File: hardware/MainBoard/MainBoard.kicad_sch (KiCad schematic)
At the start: 8 parts, among them J1 MPU9250, J2 Micro_SD_Card, J3 Servo, J4 Relay, J5 MotorDriver, J6 PicoBATT+, J7 Tachometer

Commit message: 色々つけて、フットプリント割り当てた。
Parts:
- removed J2: Micro_SD_Card, symbol Connector:Micro_SD_Card
- added D101: Relay, LED_THT:LED_D3.0mm, symbol Device:LED
- added D102: STAT, LED_THT:LED_D3.0mm, symbol Device:LED
- added D103: ERROR, LED_THT:LED_D3.0mm, symbol Device:LED
- added D104: VPP, LED_THT:LED_D3.0mm, symbol Device:LED
- added D105: VDD, LED_THT:LED_D3.0mm, symbol Device:LED
- added R101, R102, R103, R104, R105: 1k, Resistor_THT:R_Axial_DIN0204_L3.6mm_D1.6mm_P5.08mm_Horizontal, symbol Device:R
- added SW101: Reset, Button_Switch_THT:SW_PUSH_6mm, symbol Switch:SW_Push
- added SW102: SW_Pico, Button_Switch_THT:SW_Slide_SPDT_Angled_CK_OS102011MA1Q, symbol Switch:SW_SPDT
- added SW103: SW_BATT, Button_Switch_THT:SW_Slide_SPDT_Angled_CK_OS102011MA1Q, symbol Switch:SW_SPDT
- J101: renamed from J3; footprint (none) -> Connector_JST:JST_XH_B3B-XH-A_1x03_P2.50mm_Vertical
- J102: renamed from J4; footprint (none) -> Connector_JST:JST_XH_B3B-XH-A_1x03_P2.50mm_Vertical
- J103: renamed from J5; footprint (none) -> Connector_JST:JST_XH_B5B-XH-A_1x05_P2.50mm_Vertical
- J104: renamed from J1; footprint (none) -> Connector_JST:JST_XH_B10B-XH-A_1x10_P2.50mm_Vertical
- J105: renamed from J6; footprint (none) -> Connector_JST:JST_PH_B2B-PH-K_1x02_P2.00mm_Vertical
- J106: renamed from J7; footprint (none) -> Connector_JST:JST_XH_B4B-XH-A_1x04_P2.50mm_Vertical
- renumbered A1 to A101
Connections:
- net GND: now also R101.1, R102.1, R103.2, R104.2, R105.2, SW101.1, SW102.2 (B)
- net OUT1: now also A101.26 (GPIO20); no longer A101.29 (GPIO22)
- net OUT2: now also A101.27 (GPIO21); no longer A101.31 (GPIO26_ADC0)
- net Relay_S: now also D101.2 (A)
- net VDD: now also D105.2 (A)
- net at J105.1 (Pin_1): now also D104.2 (A), SW103.1 (A); no longer A101.39 (VSYS)
- net ERROR: now reaches A101.10 (GPIO7)
- net ERROR: now also D103.2 (A)
- net at A101.30 (RUN): now also SW101.2
- net at A101.37 (3V3_EN): now also SW102.1 (A)
- net STAT: now reaches A101.9 (GPIO6)
- net STAT: now also D102.2 (A)
- new net: D105.1 (K), R105.1
- new net: D103.1 (K), R103.1
- new net: D102.1 (K), R102.2
- new net: D101.1 (K), R101.2
- new net: D104.1 (K), R104.1
- new net: A101.39 (VSYS), SW103.2 (B)
- no-connect marks 21 -> 16
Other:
- added sheet microSD (untitled.kicad_sch)
- moved on the sheet: A101, J101, J102, J103, J104, J105, J106

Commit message: PCB途中
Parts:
- added B101: ~, WOBCLibrary:Board_1U_60x60, symbol WOBCLibrary:Board
- J104: footprint Connector_JST:JST_XH_B10B-XH-A_1x10_P2.50mm_Vertical -> Connector_PinSocket_2.54mm:PinSocket_1x10_P2.54mm_Vertical
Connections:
- net GND: now also B101.GND
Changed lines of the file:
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@@
 	(wire
 		(pts
+			(xy 45.72 33.02) (xy 59.69 33.02)
+		)
+		(stroke
+			(width 0)
+			(type default)
+		)
+	)
+	(wire
+		(pts
 			(xy 201.93 113.03) (xy 201.93 123.19)
 		)
@@
 	(wire
 		(pts
+			(xy 59.69 33.02) (xy 59.69 40.64)
+		)
+		(stroke
+			(width 0)
+			(type default)
+		)
+	)
+	(wire
+		(pts
 			(xy 93.98 110.49) (xy 121.92 110.49)
 		)
@@
 	(wire
 		(pts
+			(xy 45.72 40.64) (xy 45.72 33.02)
+		)
+		(stroke
+			(width 0)
+			(type default)
+		)
+	)
+	(wire
+		(pts
 			(xy 167.64 90.17) (xy 179.07 90.17)
 		)
@@
 	)
 	(symbol
+		(lib_id "WOBCLibrary:Board")
+		(at 45.72 40.64 0)
+		(unit 1)
+		(exclude_from_sim no)
+		(in_bom yes)
+		(on_board yes)
+		(dnp no)
+		(fields_autoplaced yes)
+		(property "Reference" "B101"
+			(at 48.26 40.4367 0)
+			(effects
+				(font
+					(size 1.27 1.27)
+				)
+				(justify left)
+			)
+		)
+		(property "Value" "~"
+			(at 48.26 42.9767 0)
+			(effects
+				(font
+					(size 1.27 1.27)
+				)
+				(justify left)
+			)
+		)
+		(property "Footprint" "WOBCLibrary:Board_1U_60x60"
+			(at 45.72 40.64 0)
+			(effects
+				(font
+					(size 1.27 1.27)
+				)
+				(hide yes)
+			)
+		)
+		(property "Datasheet" ""
+			(at 45.72 40.64 0)
+			(effects
+				(font
+					(size 1.27 1.27)
+				)
+				(hide yes)
+			)
+		)
+		(property "Description" ""
+			(at 45.72 40.64 0)
+			(effects
+				(font
+					(size 1.27 1.27)
+				)
+				(hide yes)
+			)
+		)
+		(pin "GND"
+		)
+		(instances
+			(project ""
+				(path "/11ae0773-063e-421c-b359-668d7833fea8"
+					(reference "B101")
+					(unit 1)
+				)
+			)
+		)
+	)
+	(symbol
 		(lib_id "power:GND")
 		(at 191.77 111.76 0)
@@
 	)
 	(symbol
+		(lib_id "power:GND")
+		(at 59.69 40.64 0)
+		(unit 1)
+		(exclude_from_sim no)
+		(in_bom yes)
+		(on_board yes)
+		(dnp no)
+		(fields_autoplaced yes)
+		(property "Reference" "#PWR0206"
+			(at 59.69 46.99 0)
+			(effects
+				(font
+					(size 1.27 1.27)
+				)
+				(hide yes)
+			)
+		)
+		(property "Value" "GND"
+			(at 59.69 45.72 0)
+			(effects
+				(font
+					(size 1.27 1.27)
+				)
+			)
+		)
+		(property "Footprint" ""
+			(at 59.69 40.64 0)
+			(effects
+				(font
+					(size 1.27 1.27)
+				)
+				(hide yes)
+			)
+		)
+		(property "Datasheet" ""
+			(at 59.69 40.64 0)
+			(effects
+				(font
+					(size 1.27 1.27)
+				)
+				(hide yes)
+			)
+		)
+		(property "Description" "Power symbol creates a global label with name \"GND\" , ground"
+			(at 59.69 40.64 0)
+			(effects
+				(font
+					(size 1.27 1.27)
+				)
+				(hide yes)
+			)
+		)
+		(pin "1"
+		)
+		(instances
+			(project ""
+				(path "/11ae0773-063e-421c-b359-668d7833fea8"
+					(reference "#PWR0206")
+					(unit 1)
+				)
+			)
+		)
+	)
+	(symbol
 		(lib_id "Connector_Generic:Conn_01x10")
 		(at 124.46 147.32 0)
@@
 			)
 		)
-		(property "Footprint" "Connector_JST:JST_XH_B10B-XH-A_1x10_P2.50mm_Vertical"
+		(property "Footprint" "Connector_PinSocket_2.54mm:PinSocket_1x10_P2.54mm_Vertical"
 			(at 124.46 147.32 0)
 			(effects

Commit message: コネクタ類をまとめた
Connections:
- net CLK: now also A101.22 (GPIO17); no longer A101.24 (GPIO18)
- net CS: now also A101.25 (GPIO19); no longer A101.22 (GPIO17)
- net MOSI: now also A101.24 (GPIO18); no longer A101.25 (GPIO19)
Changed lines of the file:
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@@
-		)
-	)
-	(label "MOSI"
-		(at 196.85 87.63 180)
-		(effects
-			(font
-				(size 1.27 1.27)
-			)
-			(justify right bottom)
 		)
 	)
@@
 		)
 	)
+	(label "CS"
+		(at 196.85 87.63 180)
+		(effects
+			(font
+				(size 1.27 1.27)
+			)
+			(justify right bottom)
+		)
+	)
 	(label "ERROR"
 		(at 59.69 168.91 180)
@@
 		)
 	)
+	(label "MOSI"
+		(at 196.85 85.09 180)
+		(effects
+			(font
+				(size 1.27 1.27)
+			)
+			(justify right bottom)
+		)
+	)
+	(label "IN2"
+		(at 93.98 107.95 0)
+		(effects
+			(font
+				(size 1.27 1.27)
+			)
+			(justify left bottom)
+		)
+	)
+	(label "Servo_S"
+		(at 88.9 127 180)
+		(effects
+			(font
+				(size 1.27 1.27)
+			)
+			(justify right bottom)
+		)
+	)
+	(label "IN1"
+		(at 88.9 93.98 180)
+		(effects
+			(font
+				(size 1.27 1.27)
+			)
+			(justify right bottom)
+		)
+	)
+	(label "Relay_S"
+		(at 59.69 146.05 180)
+		(effects
+			(font
+				(size 1.27 1.27)
+			)
+			(justify right bottom)
+		)
+	)
+	(label "ERROR"
+		(at 114.3 95.25 0)
+		(effects
+			(font
+				(size 1.27 1.27)
+			)
+			(justify left bottom)
+		)
+	)
+	(label "Servo_S"
+		(at 93.98 102.87 0)
+		(effects
+			(font
+				(size 1.27 1.27)
+			)
+			(justify left bottom)
+		)
+	)
+	(label "CS"
+		(at 201.93 73.66 0)
+		(effects
+			(font
+				(size 1.27 1.27)
+			)
+			(justify left bottom)
+		)
+	)
+	(label "STAT"
+		(at 114.3 92.71 0)
+		(effects
+			(font
+				(size 1.27 1.27)
+			)
+			(justify left bottom)
+		)
+	)
+	(label "CLK"
+		(at 196.85 82.55 180)
+		(effects
+			(font
+				(size 1.27 1.27)
+			)
+			(justify right bottom)
+		)
+	)
+	(label "FSYNC"
+		(at 113.03 160.02 0)
+		(effects
+			(font
+				(size 1.27 1.27)
+			)
+			(justify left bottom)
+		)
+	)
 	(label "MISO"
 		(at 196.85 80.01 180)
@@
 		)
 	)
-	(label "IN2"
-		(at 93.98 107.95 0)
-		(effects
-			(font
-				(size 1.27 1.27)
-			)
-			(justify left bottom)
-		)
-	)
-	(label "CS"
-		(at 196.85 82.55 180)
-		(effects
-			(font
-				(size 1.27 1.27)
-			)
-			(justify right bottom)
-		)
-	)
-	(label "Servo_S"
-		(at 88.9 127 180)
-		(effects
-			(font
-				(size 1.27 1.27)
-			)
-			(justify right bottom)
-		)
-	)
-	(label "IN1"
-		(at 88.9 93.98 180)
-		(effects
-			(font
-				(size 1.27 1.27)
-			)
-			(justify right bottom)
-		)
-	)
-	(label "Relay_S"
-		(at 59.69 146.05 180)
-		(effects
-			(font
-				(size 1.27 1.27)
-			)
-			(justify right bottom)
-		)
-	)
-	(label "ERROR"
-		(at 114.3 95.25 0)
-		(effects
-			(font
-				(size 1.27 1.27)
-			)
-			(justify left bottom)
-		)
-	)
-	(label "CLK"
-		(at 196.85 85.09 180)
-		(effects
-			(font
-				(size 1.27 1.27)
-			)
-			(justify right bottom)
-		)
-	)
-	(label "Servo_S"
-		(at 93.98 102.87 0)
-		(effects
-			(font
-				(size 1.27 1.27)
-			)
-			(justify left bottom)
-		)
-	)
-	(label "CS"
-		(at 201.93 73.66 0)
-		(effects
-			(font
-				(size 1.27 1.27)
-			)
-			(justify left bottom)
-		)
-	)
-	(label "STAT"
-		(at 114.3 92.71 0)
-		(effects
-			(font
-				(size 1.27 1.27)
-			)
-			(justify left bottom)
-		)
-	)
-	(label "FSYNC"
-		(at 113.03 160.02 0)
-		(effects
-			(font
-				(size 1.27 1.27)
-			)
-			(justify left bottom)
-		)
-	)

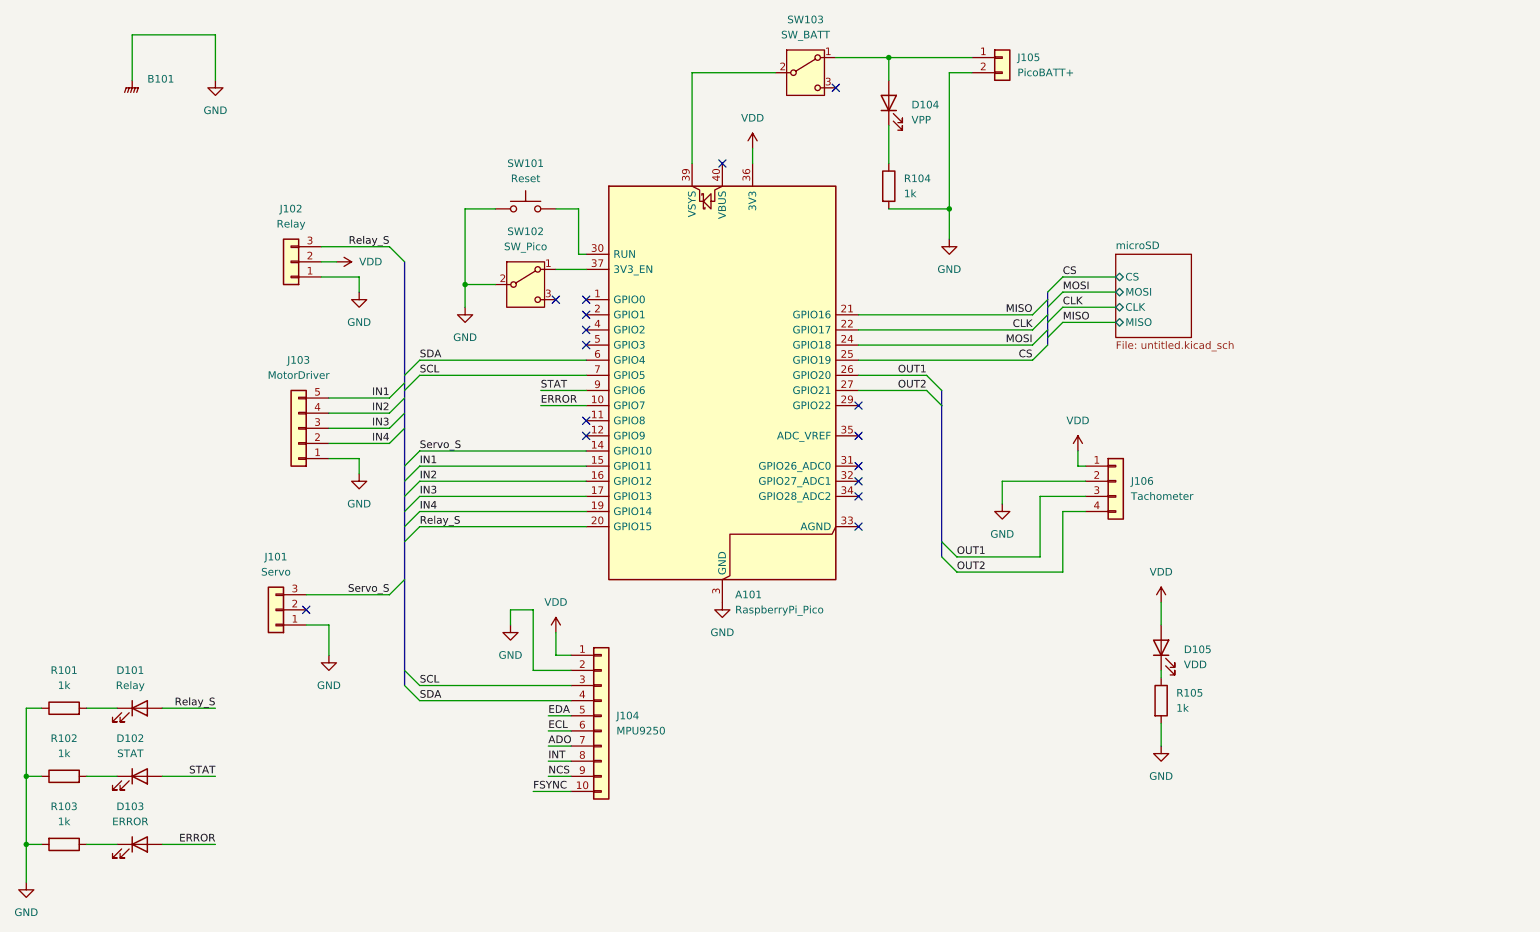
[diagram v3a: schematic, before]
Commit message: PCBで配線少し
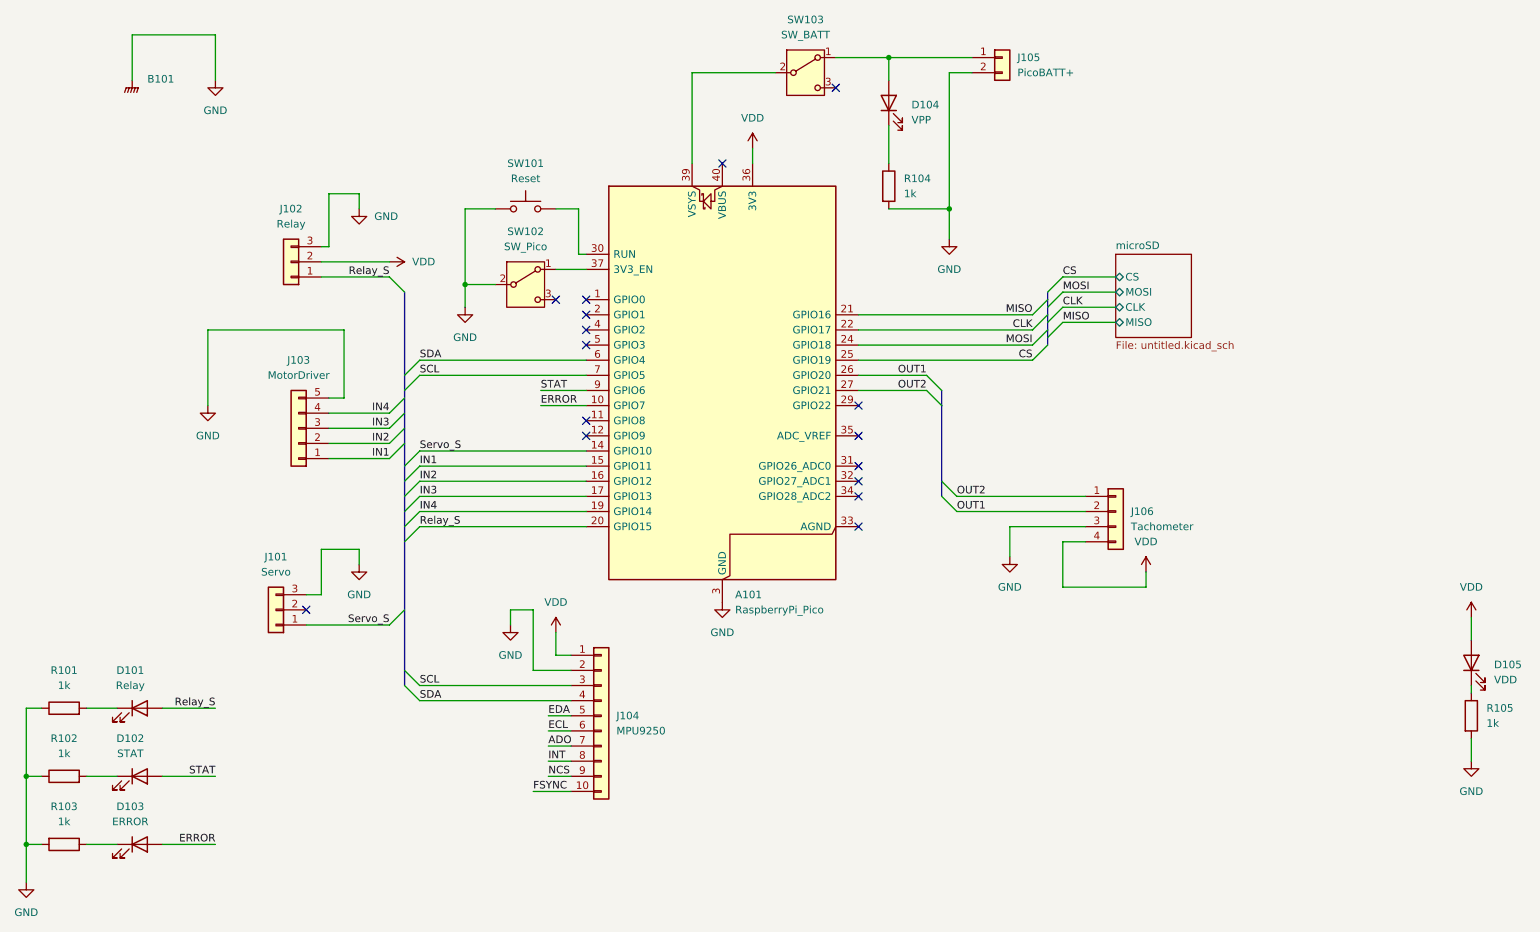
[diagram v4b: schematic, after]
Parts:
- J101, J102: footprint Connector_JST:JST_XH_B3B-XH-A_1x03_P2.50mm_Vertical -> Connector_JST:JST_XA_S03B-XASK-1_1x03_P2.50mm_Horizontal
- J103: footprint Connector_JST:JST_XH_B5B-XH-A_1x05_P2.50mm_Vertical -> Connector_JST:JST_XA_S05B-XASK-1_1x05_P2.50mm_Horizontal
- J106: footprint Connector_JST:JST_XH_B4B-XH-A_1x04_P2.50mm_Vertical -> Connector_JST:JST_XA_S04B-XASK-1_1x04_P2.50mm_Horizontal
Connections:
- net GND: now also J101.3 (Pin_3), J102.3 (Pin_3), J103.5 (Pin_5), J106.3 (Pin_3); no longer J101.1 (Pin_1), J102.1 (Pin_1), J103.1 (Pin_1), J106.2 (Pin_2)
- net IN1: now also J103.1 (Pin_1); no longer J103.5 (Pin_5)
- net IN2: now also J103.2 (Pin_2); no longer J103.4 (Pin_4)
- net IN4: now also J103.4 (Pin_4); no longer J103.2 (Pin_2)
- net OUT1: now also J106.2 (Pin_2); no longer J106.3 (Pin_3)
- net OUT2: now also J106.1 (Pin_1); no longer J106.4 (Pin_4)
- net Relay_S: now also J102.1 (Pin_1); no longer J102.3 (Pin_3)
- net Servo_S: now also J101.1 (Pin_1); no longer J101.3 (Pin_3)
- net VDD: now also J106.4 (Pin_4); no longer J106.1 (Pin_1)
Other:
- moved on the sheet: D105, J106, R105

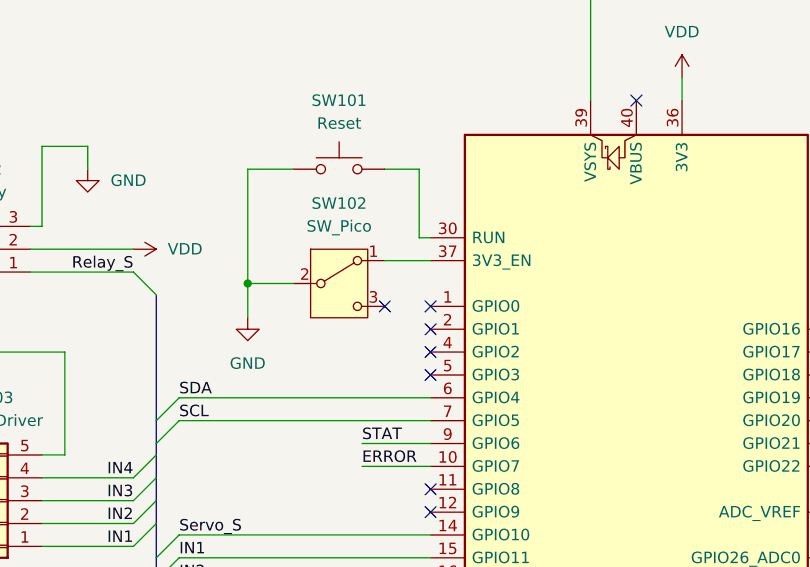
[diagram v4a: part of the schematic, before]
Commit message: スイッチの配線を変更
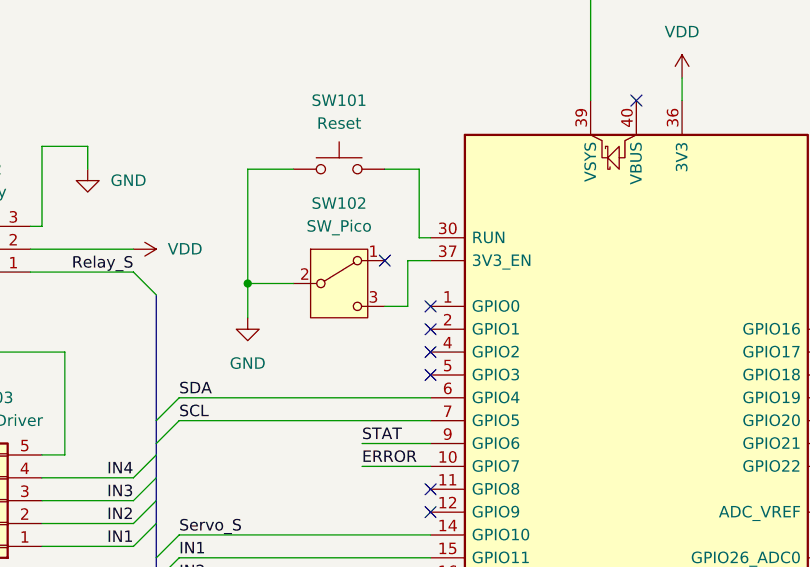
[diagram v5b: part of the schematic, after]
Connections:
- net at SW102.1 (A): no longer A101.37 (3V3_EN)
- net at SW102.3 (C): now also A101.37 (3V3_EN)
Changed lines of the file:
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@@
 	)
 	(no_connect
-		(at 116.84 77.47)
+		(at 116.84 72.39)
 	)
 	(no_connect
@@
 	(wire
 		(pts
-			(xy 116.84 72.39) (xy 121.92 72.39)
-		)
-		(stroke
-			(width 0)
-			(type default)
-		)
-	)
-	(wire
-		(pts
 			(xy 201.93 125.73) (xy 215.9 125.73)
 		)
@@
 	(wire
 		(pts
+			(xy 119.38 77.47) (xy 116.84 77.47)
+		)
+		(stroke
+			(width 0)
+			(type default)
+		)
+	)
+	(wire
+		(pts
 			(xy 43.18 157.48) (xy 38.1 157.48)
 		)
@@
 	(wire
 		(pts
+			(xy 119.38 72.39) (xy 119.38 77.47)
+		)
+		(stroke
+			(width 0)
+			(type default)
+		)
+	)
+	(wire
+		(pts
 			(xy 120.65 69.85) (xy 121.92 69.85)
 		)
@@
 		)
 		(stroke
+			(width 0)
+			(type default)
+		)
+	)
+	(wire
+		(pts
+			(xy 121.92 72.39) (xy 119.38 72.39)
+		)
+		(stroke

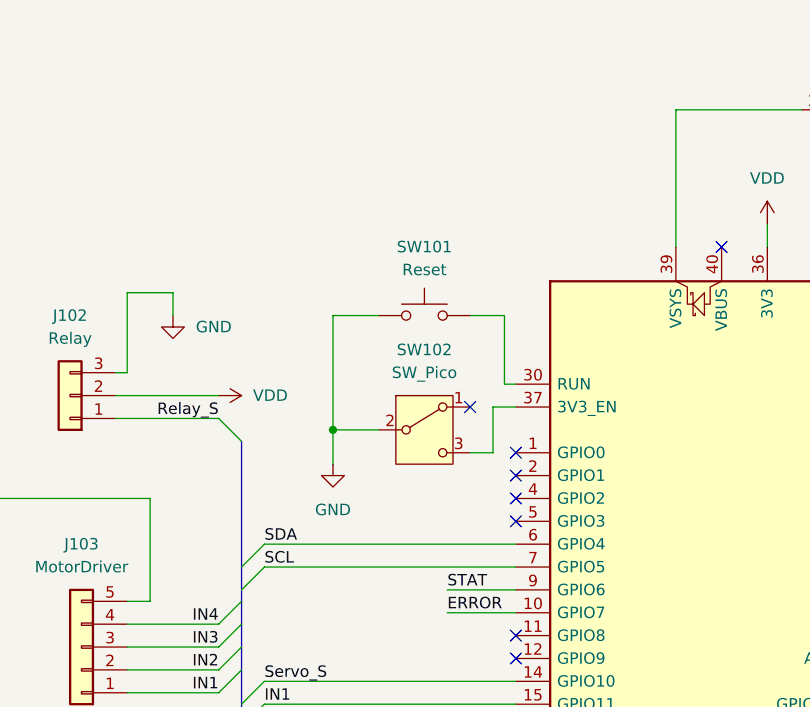
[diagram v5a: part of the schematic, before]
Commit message: シルク追加してちょっと配線変更
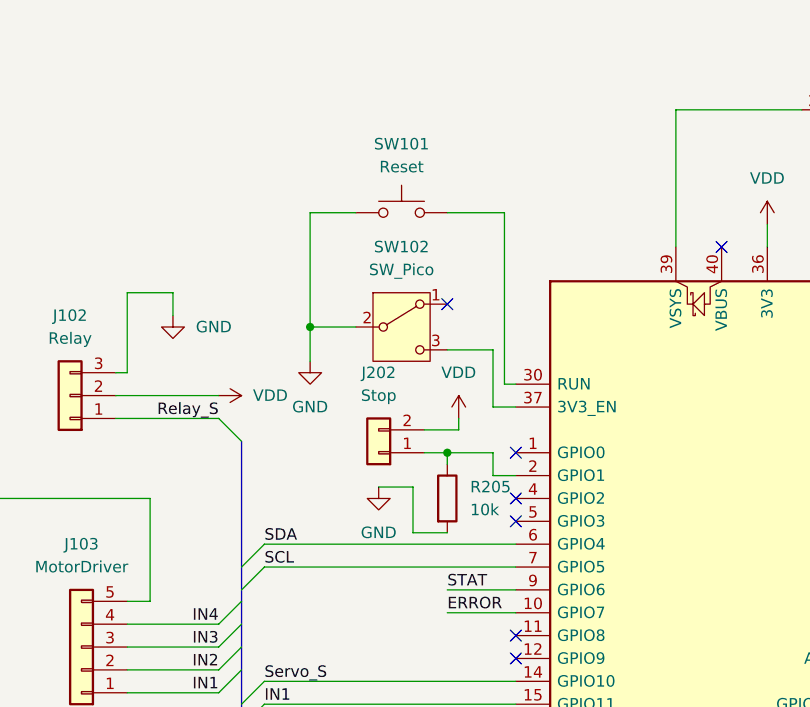
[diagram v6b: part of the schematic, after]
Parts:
- added J202: Stop, Connector_JST:JST_PH_B2B-PH-K_1x02_P2.00mm_Vertical, symbol Connector_Generic:Conn_01x02
- added R205: 10k, Resistor_THT:R_Axial_DIN0204_L3.6mm_D1.6mm_P5.08mm_Horizontal, symbol Device:R
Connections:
- net GND: now also R205.2
- net VDD: now also J202.2 (Pin_2)
- net at A101.2 (GPIO1): now also J202.1 (Pin_1), R205.1
- no-connect marks 16 -> 15
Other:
- moved on the sheet: SW101, SW102
